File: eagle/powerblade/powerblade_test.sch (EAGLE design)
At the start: 85 parts, among them J1 JTAG_14PIN_IDC-NL, J21 AC_INFILM, Q1 2N7002, U1 TPS62122, U2 AD524, U3 MSP430FR5738, U4 LTC5800, U5 MAX9910, U6 MAX9910, X1 ABM8G, X2 ABS07, Y1 UREACH_XTEND

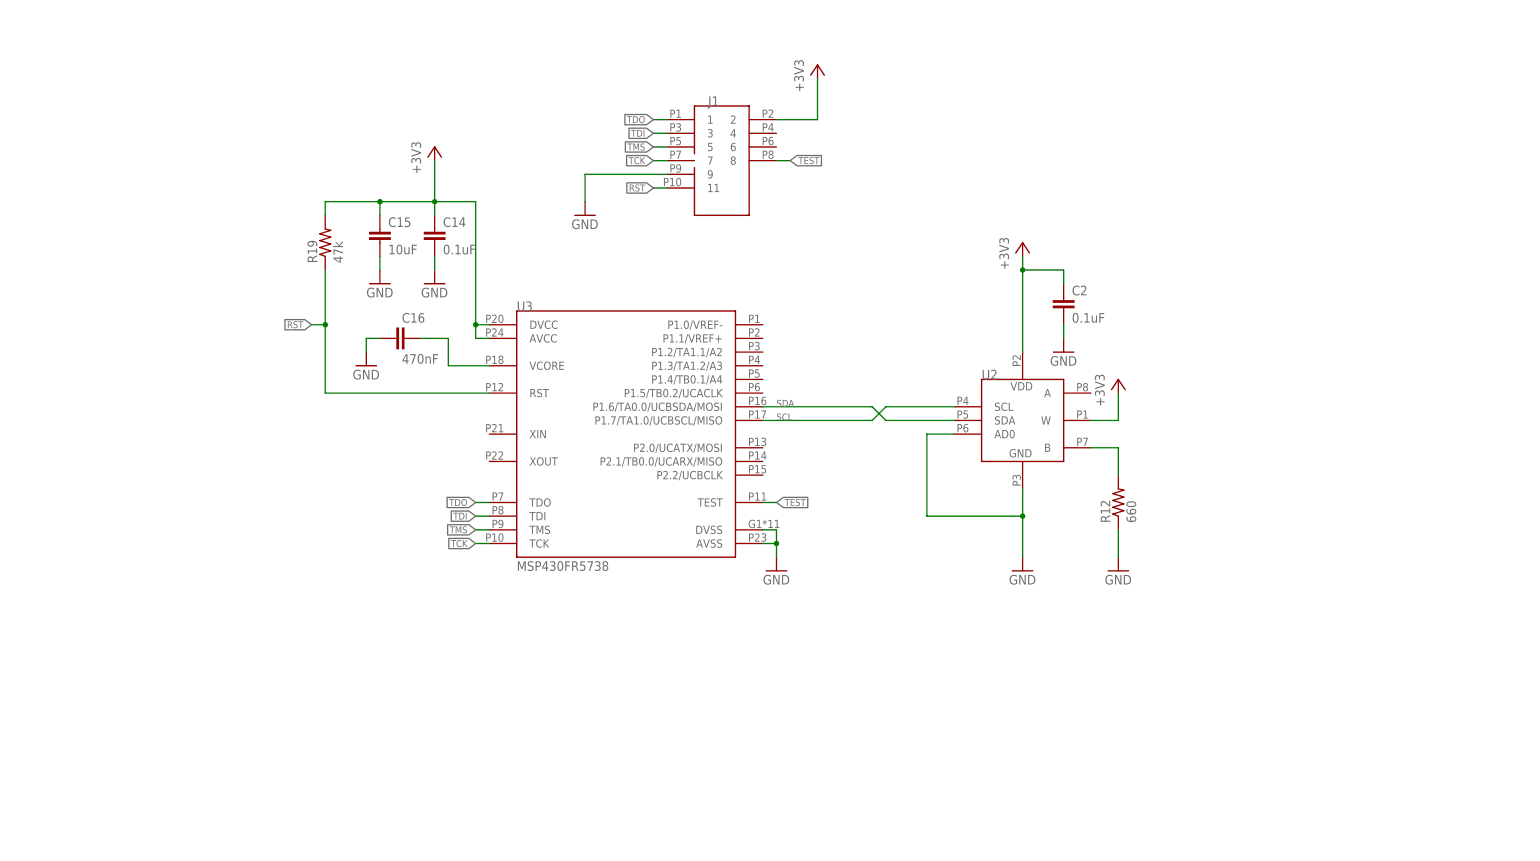
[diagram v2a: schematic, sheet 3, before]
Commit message: added tr1000 to powerblade test sch
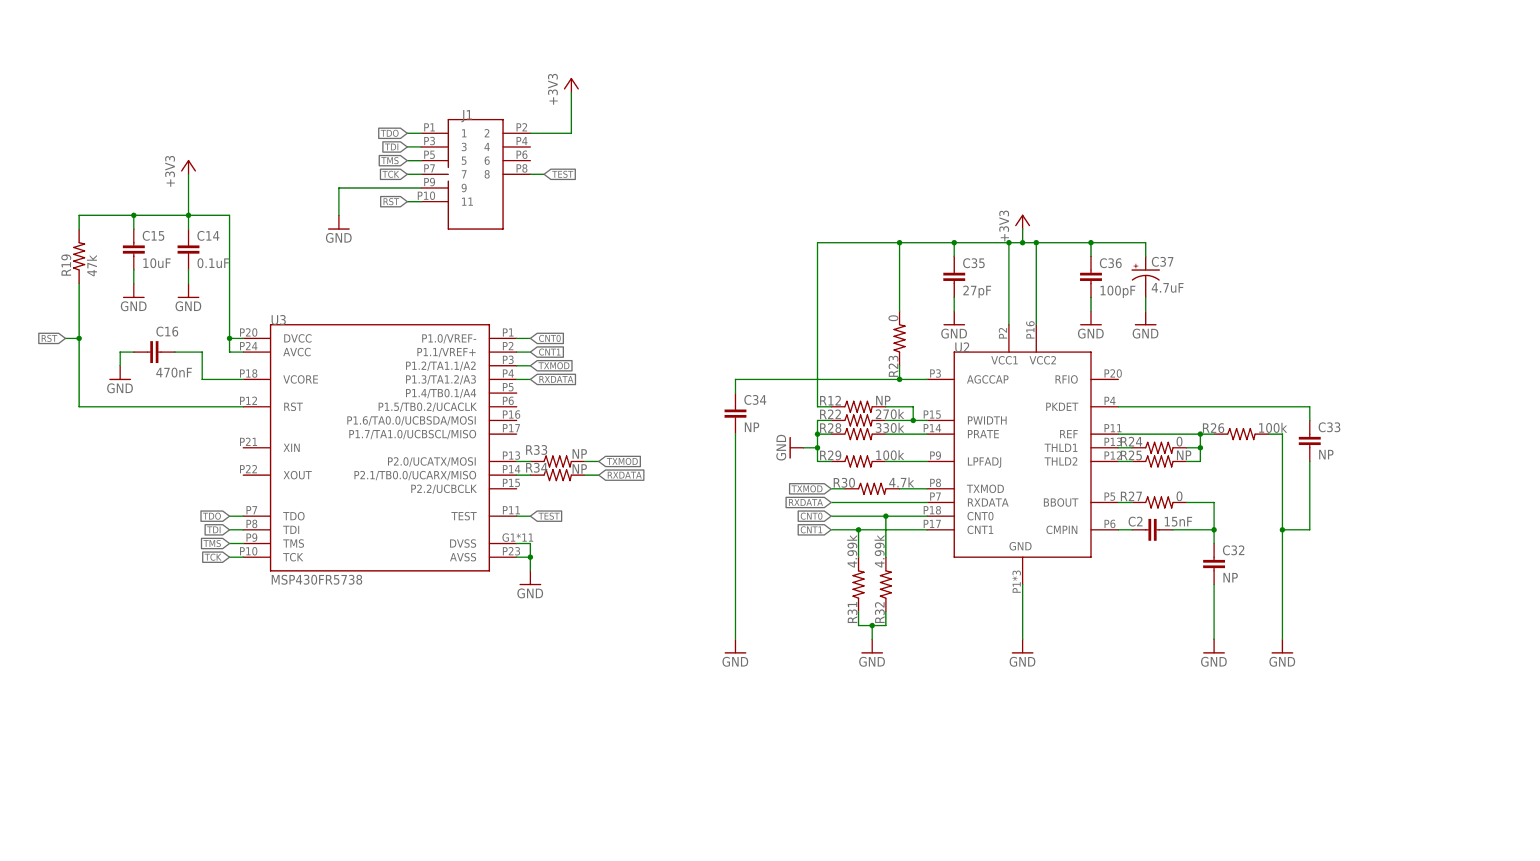
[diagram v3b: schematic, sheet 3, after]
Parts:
- added C32, C33, C34: NP, rcl:C-EUC0603
- added C35: 27pF, rcl:C-EUC0603
- added C36: 100pF, rcl:C-EUC0603
- added C37: 4.7uF, rcl:CPOL-US0805
- added R22: 270k, rcl:R-US_R0603
- added R23, R24, R27: 0, rcl:R-US_R0603
- added R25, R33, R34: NP, rcl:R-US_R0603
- added R26, R29: 100k, rcl:R-US_R0603
- added R28: 330k, rcl:R-US_R0603
- added R30: 4.7k, rcl:R-US_R0603
- added R31, R32: 4.99k, rcl:R-US_R0603
- C2: value 0.1uF -> 15nF; DIGIKEY 445-1316-1-ND -> (none)
- R12: value 660 -> NP; DIGIKEY P665HCT-ND -> (none)
- U2: value AD524 -> TR1000; device powerfilm:AD524 -> powerfilm:TR1000
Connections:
- removed net SCL: U2.SCL, U3.P1.7/TA1.0/UCBSCL/MISO
- removed net SDA: U2.SDA, U3.P1.6/TA0.0/UCBSDA/MOSI
- new net CNT0: R32.2, U2.CNT0, U3.P1.0/VREF-
- new net CNT1: R31.2, U2.CNT1, U3.P1.1/VREF+
- new net N$49: C34.1, R23.1, U2.AGCCAP
- new net N$50: R12.2, R22.2, U2.PWIDTH
- new net N$51: R28.2, U2.PRATE
- new net N$52: R29.2, U2.LPFADJ
- new net N$53: R30.2, U2.TXMOD
- new net N$54: C2.2, C32.1, R27.2
- new net N$55: C2.1, U2.CMPIN
- new net N$56: R24.2, R25.2, R26.1, U2.REF
- new net N$57: R24.1, U2.THLD1
- new net N$58: R25.1, U2.THLD2
- new net N$59: C33.1, U2.PKDET
- new net N$60: R33.1, U3.P2.0/UCATX/MOSI
- new net N$61: R34.1, U3.P2.1/TB0.0/UCARX/MISO
- new net RXDATA: R34.2, U2.RXDATA, U3.P1.3/TA1.2/A3
- new net TXMOD: R30.1, R33.2, U3.P1.2/TA1.1/A2
- net +3V3: now also C35.1, C36.1, C37.+, R12.1, R23.2, U2.VCC1, U2.VCC2; no longer C2.1, U2.VDD, U2.W
- net GND: now also C32.2, C33.2, C34.2, C35.2, C36.2, C37.-, R22.1, R26.2, R28.1, R29.1, R31.1, R32.1; no longer C2.2, R12.1, U2.AD0
- net N$12: now also R27.1, U2.BBOUT; no longer R12.2, U2.B
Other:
- moved on the sheet: C14, C15, C16, C2, J1, R12, R19, U3

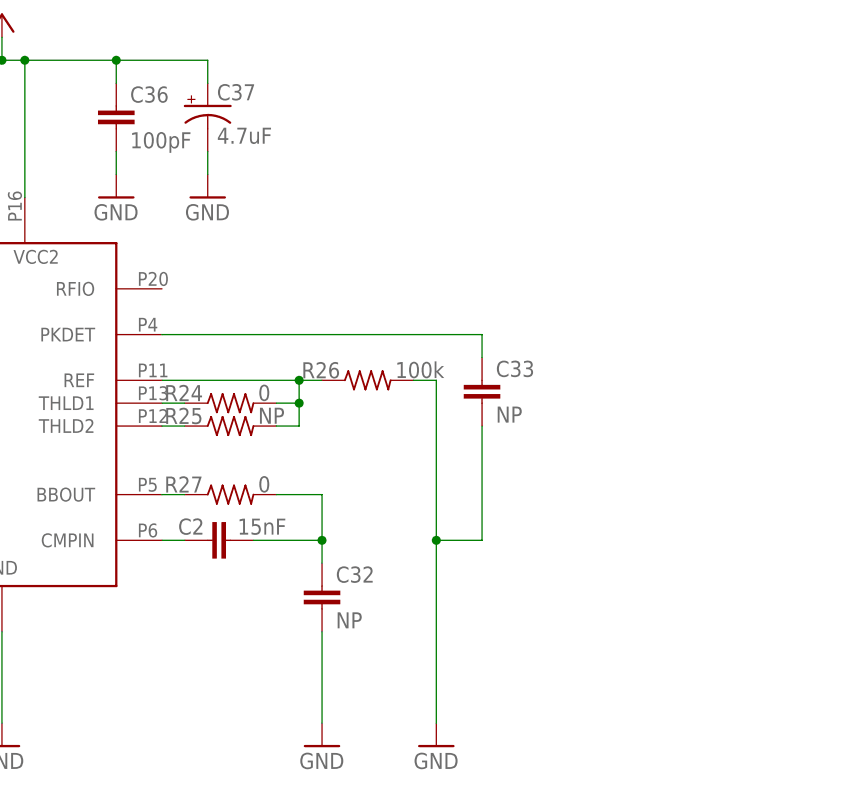
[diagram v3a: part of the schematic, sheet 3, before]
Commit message: added antenna to tr1000 circuit
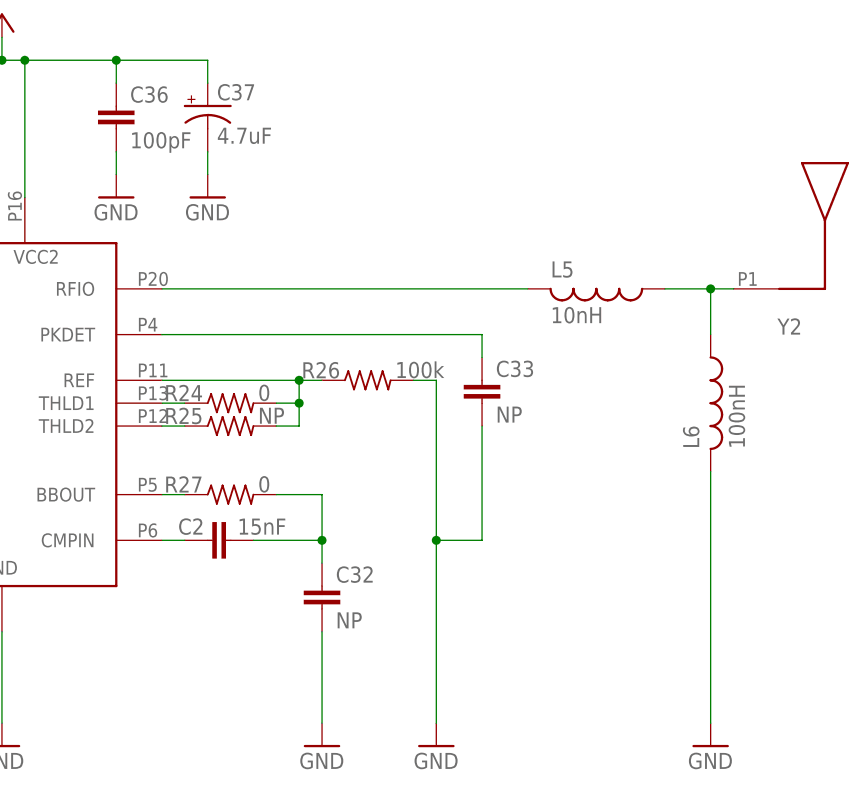
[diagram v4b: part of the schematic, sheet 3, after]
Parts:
- added L5: 10nH, rcl:L-USL0402
- added L6: 100nH, rcl:L-USL0402
- added Y2: ANT-916, powerfilm:ANT-916
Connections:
- new net N$62: L5.2, U2.RFIO
- new net N$63: L5.1, L6.1, Y2.P1
- net GND: now also L6.2
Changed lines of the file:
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@@
 <part name="R26" library="rcl" deviceset="R-US_" device="R0603" value="100k"/>
 <part name="R27" library="rcl" deviceset="R-US_" device="R0603" value="0"/>
+<part name="L5" library="rcl" deviceset="L-US" device="L0402" value="10nH"/>
+<part name="L6" library="rcl" deviceset="L-US" device="L0402" value="100nH"/>
+<part name="Y2" library="powerfilm" deviceset="ANT-916" device=""/>
+<part name="GND42" library="supply1" deviceset="GND" device=""/>
 </parts>
 <sheets>
@@
 <attribute name="VALUE" x="102.108" y="-14.986" size="1.778" layer="96"/>
 </instance>
+<instance part="L5" gate="G$1" x="139.7" y="7.62" rot="R270"/>
+<instance part="L6" gate="G$1" x="152.4" y="-5.08"/>
+<instance part="Y2" gate="G$1" x="165.1" y="7.62" rot="MR0"/>
+<instance part="GND42" gate="1" x="152.4" y="-43.18"/>
 </instances>
 <busses>
@@
 <pinref part="R31" gate="G$1" pin="1"/>
 <pinref part="R32" gate="G$1" pin="1"/>
+</segment>
+<segment>
+<pinref part="L6" gate="G$1" pin="2"/>
+<pinref part="GND42" gate="1" pin="GND"/>
+<wire x1="152.4" y1="-12.7" x2="152.4" y2="-40.64" width="0.1524" layer="91"/>
 </segment>
 </net>
@@
 </segment>
 </net>
+<net name="N$62" class="0">
+<segment>
+<pinref part="U2" gate="G$1" pin="RFIO"/>
+<pinref part="L5" gate="G$1" pin="2"/>
+<wire x1="91.44" y1="7.62" x2="132.08" y2="7.62" width="0.1524" layer="91"/>
+</segment>
+</net>
+<net name="N$63" class="0">
+<segment>
+<pinref part="L5" gate="G$1" pin="1"/>
+<pinref part="Y2" gate="G$1" pin="P1"/>
+<wire x1="147.32" y1="7.62" x2="152.4" y2="7.62" width="0.1524" layer="91"/>
+<pinref part="L6" gate="G$1" pin="1"/>
+<wire x1="152.4" y1="7.62" x2="154.94" y2="7.62" width="0.1524" layer="91"/>
+<wire x1="152.4" y1="2.54" x2="152.4" y2="7.62" width="0.1524" layer="91"/>
+<junction x="152.4" y="7.62"/>
+</segment>
+</net>

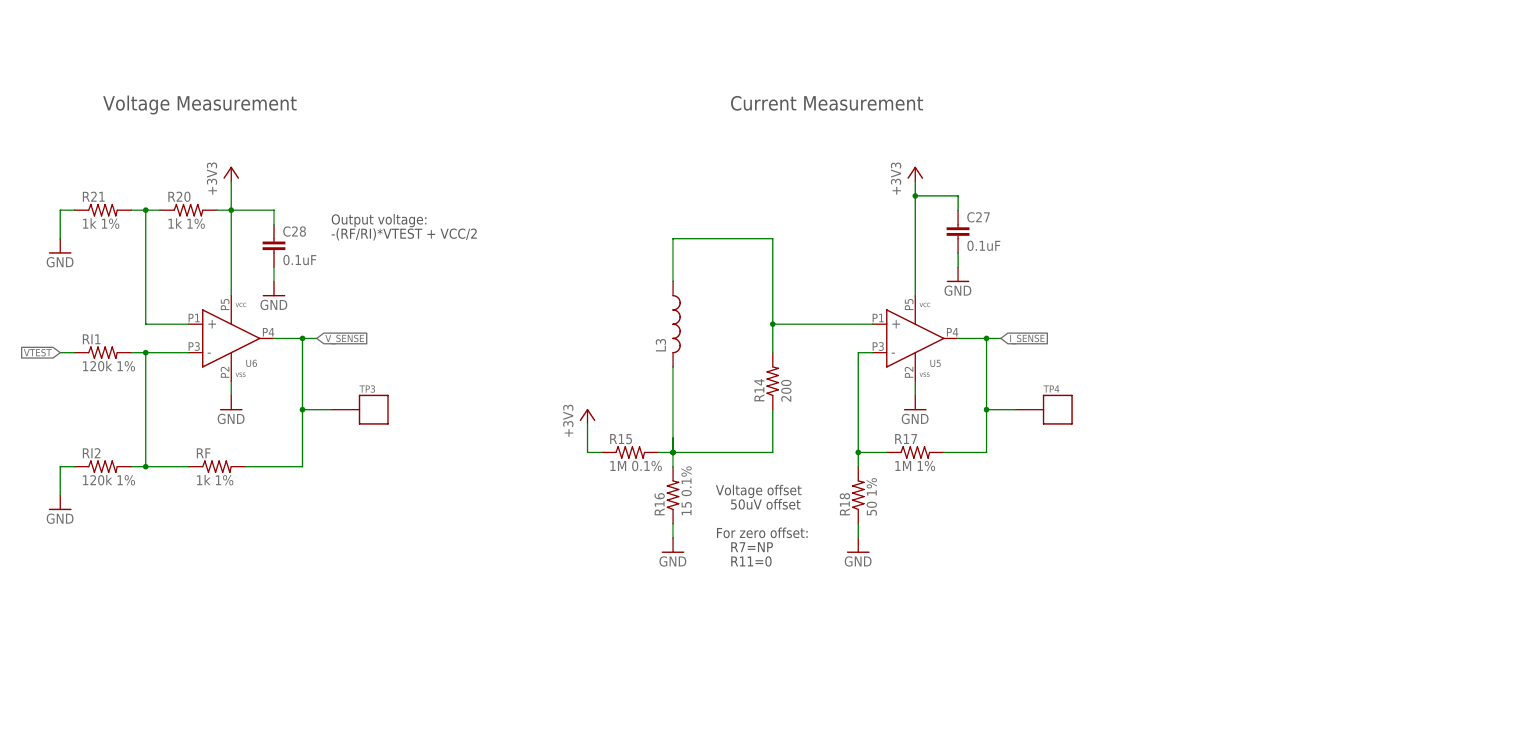
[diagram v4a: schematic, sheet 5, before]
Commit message: finished final amplifier design including high pass filter and pots for adjusting
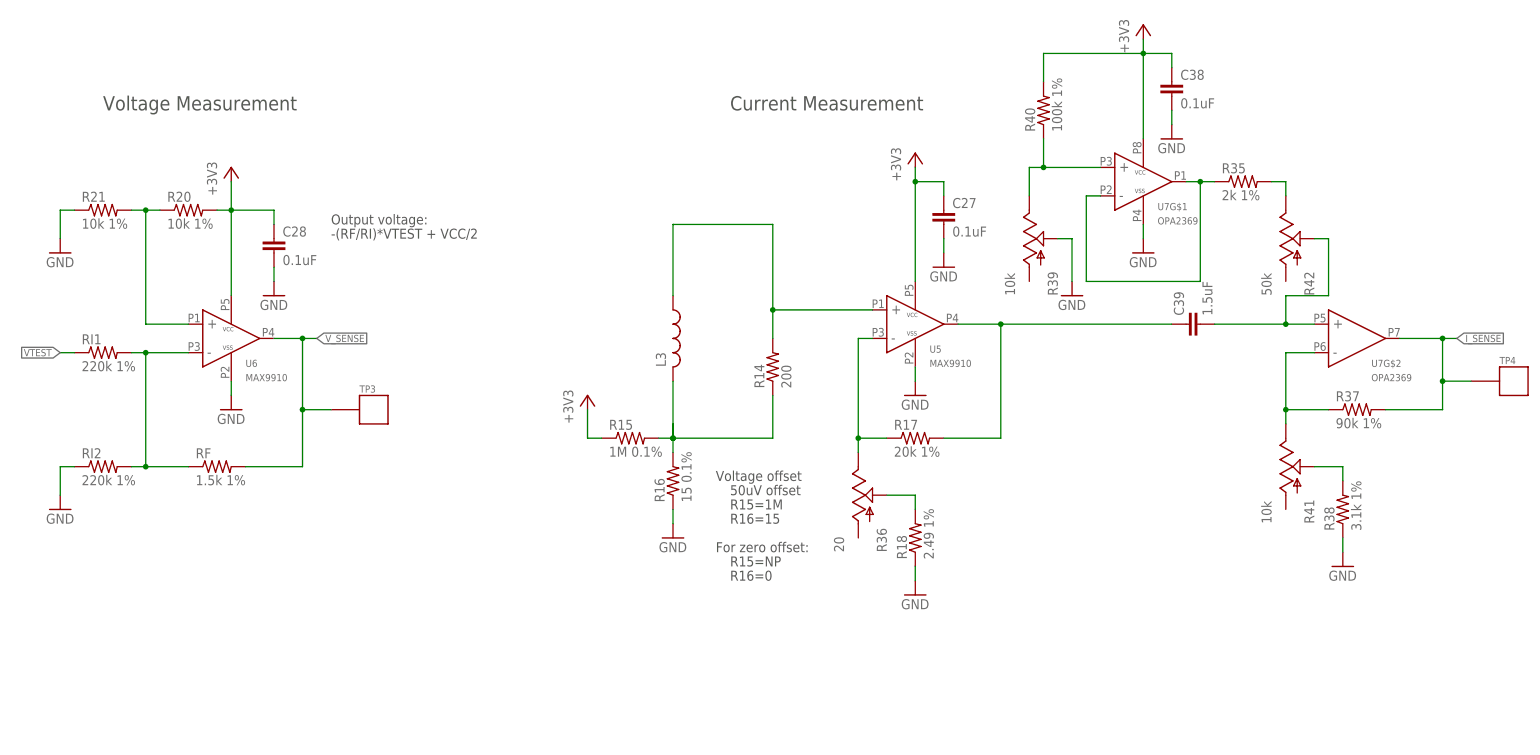
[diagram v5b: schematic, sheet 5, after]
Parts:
- added C38: 0.1uF, rcl:C-EUC0402
- added C39: 1.5uF, rcl:C-EUC0603
- added R35: 2k 1%, rcl:R-US_R0603
- added R36: 20, powerfilm:3313_POT
- added R37: 90k 1%, rcl:R-US_R0603
- added R38: 3.1k 1%, rcl:R-US_R0603
- added R39, R41: 10k, powerfilm:3313_POT
- added R40: 100k 1%, rcl:R-US_R0603
- added R42: 50k, powerfilm:3313_POT
- added U7: OPA2369, powerfilm:OPA2369
- R17: value 1M 1% -> 20k 1%
- R18: value 50 1% -> 2.49 1%
- R20, R21: value 1k 1% -> 10k 1%
- RF: value 1k 1% -> 1.5k 1%
- RI1, RI2: value 120k 1% -> 220k 1%
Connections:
- new net LTC_RCTS: U4G$3.URCTS
- new net LTC_RRTS: U4G$3.URRTS
- new net LTC_RX: U4G$3.URX
- new net LTC_TCTS: U4G$3.UTCTS
- new net LTC_TRTS: U4G$3.UTRTS
- new net LTC_TX: U4G$3.UTX
- new net N$64: C39.1, R17.2, U5.OUT
- new net N$65: R18.2, R36.PW
- new net N$66: R37.1, R41.P2, U7G$2.IN-
- new net N$67: C39.2, R42.PW, U7G$2.IN+
- new net N$68: R35.1, U7G$1.IN-, U7G$1.OUT
- new net N$69: R38.2, R41.PW
- new net N$70: R39.P2, R40.1, U7G$1.IN+
- new net N$71: R35.2, R42.P2
- net +3V3: now also C38.1, R40.2, U7G$1.VCC
- net GND: now also C38.2, R38.1, R39.PW, U7G$1.VSS
- net I_SENSE: now also R37.2, U7G$2.OUT; no longer R17.2, U5.OUT
- net N$39: now also R36.P2; no longer R18.2
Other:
- note added: "R15=1M"
- note added: "R15=NP"
- note added: "R16=0"
- note added: "R16=15"
- note removed: "R11=0"
- note removed: "R7=NP"
- moved on the sheet: C27, L3, R14, R15, R16, R17, R18, TP4, U5
